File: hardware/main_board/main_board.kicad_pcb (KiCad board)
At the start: 4 copper layers, 154 x 50 mm, 154 parts, among them J1 USB_C_Receptacle_USB2.0_16P, J2 UART_DEBUG, J3 BAT1, J4 Conn_02x05_Odd_Even, J5 Conn_02x05_Odd_Even, Q1 MMBT3904, Q10 MMBTA42, Q11 MMBTA92, Q12 MMBTA42, Q13 MMBTA92, Q14 MMBTA42, Q15 MMBTA92, Q2 MMBT3904, Q3 FDS2734, Q4 MMBTA92, Q5 MMBTA42, Q6 MMBTA42, Q7 MMBTA92, Q8 MMBTA42, Q9 MMBTA92, SW1 SW_Push, U1 MPU-6050, U10 AMS1117, U11 LM5155, U12 IP5305T, U13 74HC238, U2 CP2102N-A02-GQFN28, U3 SRV05-4, U4 DFPlayer_mini, U5 ESP32-S3-WROOM1, U6 DS3231MZ, U7 INA3221, U8 BQ27441DRZR-G1A, U9 TPS62177DQC

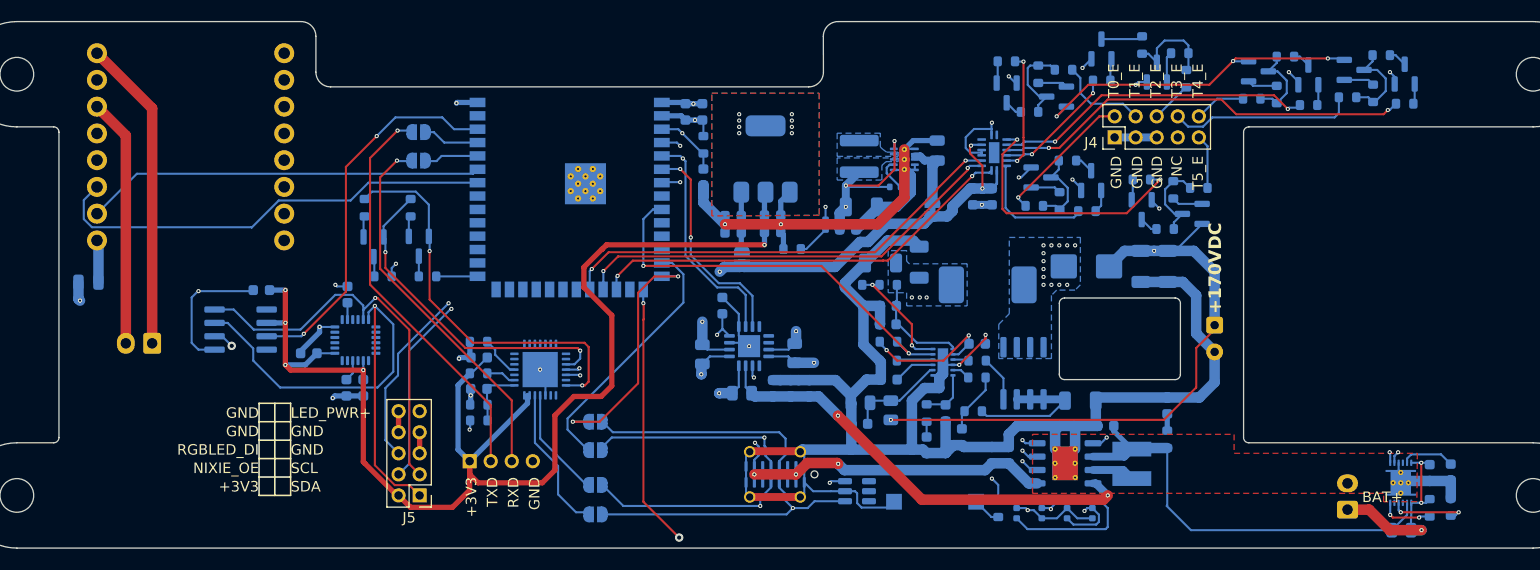
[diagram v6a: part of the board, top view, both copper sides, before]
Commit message: hardware(schematic): update main control board schematic and layout
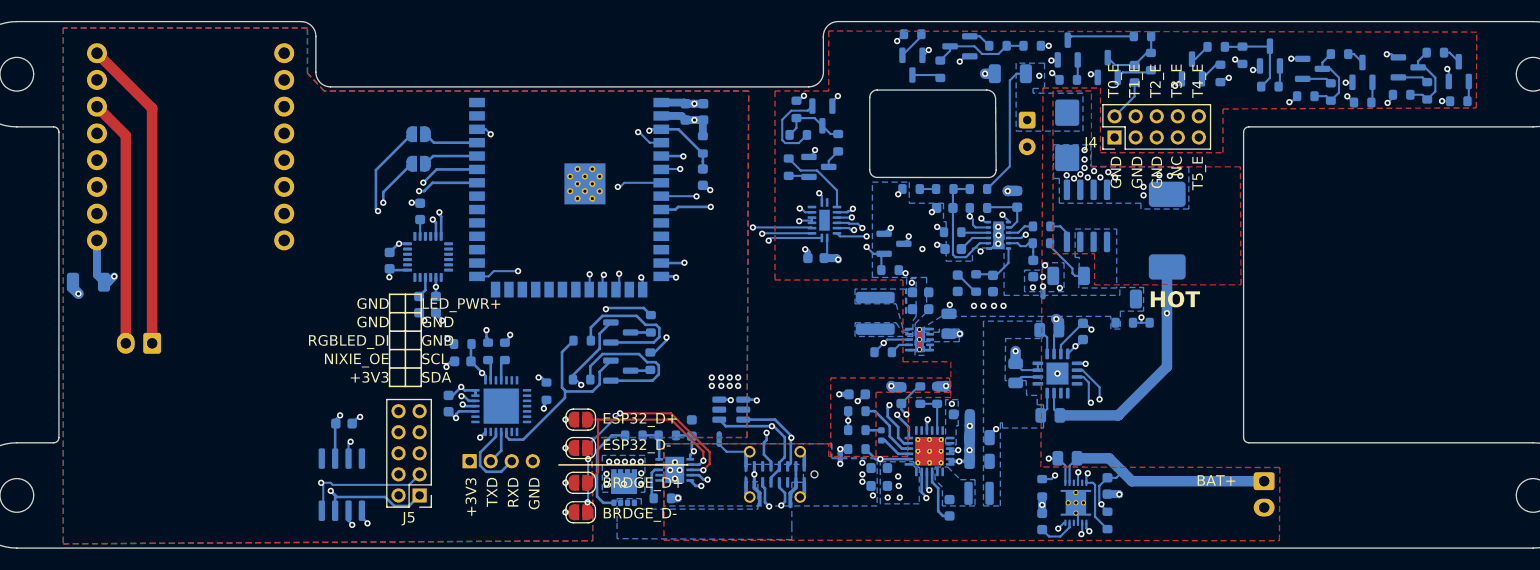
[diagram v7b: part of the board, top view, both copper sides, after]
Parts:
- removed C12, C22, C23, C28, C42, C43: 0.1u, Capacitor_SMD:C_0603_1608Metric
- removed C15: 22u, Capacitor_SMD:C_0603_1608Metric
- removed C24, C27: 10u, Capacitor_SMD:C_0603_1608Metric
- removed C26: 100u, Capacitor_SMD:C_1206_3216Metric
- removed C35: 0.47u/200V, Capacitor_SMD:C_1206_3216Metric
- removed D1, D2, D3: LED, LED_SMD:LED_0402_1005Metric
- removed D5: R_LED, LED_SMD:LED_0402_1005Metric
- removed the G*** at (97.6, 134.9)
- removed JP7: NC, Jumper:SolderJumper-2_P1.3mm_Bridged_RoundedPad1.0x1.5mm
- removed JP8: NO, Jumper:SolderJumper-2_P1.3mm_Open_RoundedPad1.0x1.5mm
- removed L1: PRS4018-2R2NT, johnson:L_SMD_4040
- removed R15: 2, Resistor_SMD:R_0603_1608Metric
- removed R22: 10k, Resistor_SMD:R_0603_1608Metric
- removed SW1: SW_Push, Button_Switch_SMD:SW_SPST_CK_RS282G05A3
- removed U12: IP5305T, Package_SO:HTSOP-8-1EP_3.9x4.9mm_P1.27mm_EP2.4x3.2mm_ThermalVias
- added C44: 4.7u, Capacitor_SMD:C_0603_1608Metric, B.Cu at (158.0, 131.5)
- added C45: 10u, Capacitor_SMD:C_0603_1608Metric, B.Cu at (163.7, 133.3)
- added C46: 10u, Capacitor_SMD:C_0805_2012Metric, B.Cu at (165.4, 137.8)
- added C47: 10u, Capacitor_SMD:C_0805_2012Metric, B.Cu at (165.4, 135.5)
- added G***: LOGO, habonroof_kicad_library:HR_logo_6mmx6mm, B.Cu at (100.2, 125.5)
- added L4: 1u, Inductor_SMD:L_Wuerth_PMCI-252010, B.Cu at (165.4, 140.8)
- added NT1: NetTie_2, NetTie:NetTie-2_SMD_Pad0.5mm, B.Cu at (152.2, 137.5)
- added NT2: NetTie_2, NetTie:NetTie-2_SMD_Pad0.5mm, B.Cu at (140.7, 135.7)
- added NT3: NetTie_2, NetTie:NetTie-2_SMD_Pad0.5mm, B.Cu at (171.4, 121.7)
- added Q16: 2N7002, Package_TO_SOT_SMD:SOT-23, B.Cu at (157.3, 117.1)
- added Q17: FDMC4435BZ, Package_SON:VSON-8_3.3x3.3mm_P0.65mm_NexFET, B.Cu at (131.7, 140.3)
- added R3: 150, Resistor_SMD:R_0603_1608Metric, B.Cu at (158.9, 111.9)
- added R4: 100k, Resistor_SMD:R_0603_1608Metric, B.Cu at (156.9, 119.6)
- added R57: 100k, Resistor_SMD:R_0603_1608Metric, B.Cu at (135.8, 135.3)
- added R58: 10k, Resistor_SMD:R_0603_1608Metric, B.Cu at (135.3, 141.3)
- added R62: 10k, Resistor_SMD:R_0603_1608Metric, B.Cu at (153.8, 136.6)
- added R63: 10k, Resistor_SMD:R_0603_1608Metric, B.Cu at (159.8, 131.5)
- added R64: 10k, Resistor_SMD:R_0603_1608Metric, B.Cu at (161.4, 131.5)
- added R66: 2.2k, Resistor_SMD:R_0603_1608Metric, B.Cu at (153.8, 134.8)
- added U14: BQ25601, Package_DFN_QFN:Texas_RTW_WQFN-24-1EP_4x4mm_P0.5mm_EP2.7x2.7mm_ThermalVias, B.Cu at (160.7, 136.8)
- C10, C11, C21: value 10u -> 1u
- C17, C4, C40, C5: value 0.1u -> 100n
- C18: value 22u -> 10u
- C20: value 22u -> 47n
- C30: value 18n -> 120n
- C31: value 33p -> 50p
- C32: value 1n -> 100n
- C39: footprint Capacitor_SMD:C_1206_3216Metric -> Capacitor_SMD:C_0603_1608Metric
- C7: value 100uF -> 100u; footprint Capacitor_SMD:C_0805_2012Metric -> Capacitor_SMD:C_1206_3216Metric
- C8: value 0.1u -> 1u
- D4: value LED -> GLED
- JP1, JP2, JP5, JP6: moved to F.Cu
- R19: footprint Resistor_SMD:R_0402_1005Metric -> Resistor_SMD:R_0603_1608Metric
- R27: value 30k -> 22k
- R28: value 0 -> 10k
- R29: value 0 -> 10
- R30: value 0 -> 100
- R31: value LMJ12MF1P0R047 -> WSLP1206R0330FEA
- R32: footprint Resistor_SMD:R_0805_2012Metric -> Resistor_SMD:R_0603_1608Metric
- R33: value 6k -> 5.6k; footprint Resistor_SMD:R_0805_2012Metric -> Resistor_SMD:R_0603_1608Metric
- U10: value AMS1117 -> HUSB238_002DD; footprint Package_TO_SOT_SMD:SOT-223-3_TabPin2 -> Package_DFN_QFN:WDFN-10-1EP_3x3mm_P0.5mm_EP1.8x2.5mm
- moved C11 78.2 mm to (105.1, 134.2), turned to 0 degrees
- moved C13 39.1 mm to (171.4, 143.5), turned to 90 degrees
- moved R56 38.9 mm to (148.0, 104.3), turned to 90 degrees
- moved R20 38.8 mm to (171.4, 140.3), turned to 90 degrees
- moved Q15 36.3 mm to (150.5, 105.0), turned to -90 degrees
- moved R55 36.0 mm to (148.2, 106.8), turned to 180 degrees
- moved R53 33.5 mm to (147.3, 109.8), turned to -90 degrees
- moved R28 33.0 mm to (132.6, 135.3), turned to 0 degrees
- moved R12 33.0 mm to (172.1, 125.3), turned to 0 degrees
- moved R16 32.4 mm to (173.8, 137.5)
- moved R54 32.1 mm to (152.0, 107.5), turned to 90 degrees
- moved Q14 30.9 mm to (150.2, 109.8), turned to 0 degrees
- moved U8 30.9 mm to (174.6, 141.7), turned to 90 degrees
- moved U10 30.8 mm to (136.5, 138.6), turned to 180 degrees
- moved C19 30.6 mm to (177.6, 140.1)
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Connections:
- C10 pad 1: Net-(U12-BAT) -> +5V
- C11 pad 1: Net-(C11-Pad1) -> +3V3
- C13 pad 2: GND -> PGND1
- C18 pad 1: +5V_CHG -> Net-(U14-PMID)
- C18 pad 2: GND -> AGND1
- C19 pad 2: GND -> PGND1
- C20 pad 1: +5V_CHG -> Net-(C20-Pad1)
- C20 pad 2: GND -> Net-(U14-BTST)
- C21 pad 1: Net-(JP8-B) -> VBUS
- C25 pad 2: GND -> PGND1
- C29 pad 2: GND -> PGND1
- C30 pad 2: GND -> PGND1
- C31 pad 2: GND -> PGND1
- C32 pad 1: Net-(C32-Pad1) -> Net-(U11-CS)
- C32 pad 2: GND -> PGND2
- C33 pad 1: GND -> PGND1
- C34 pad 2: GND -> PGND2
- C36 pad 2: GND -> PGND2
- C37 pad 2: GND -> PGND1
- C38 pad 1: Net-(JP7-B) -> +5V
- C38 pad 2: GND -> PGND1
- C39 pad 2: GND -> PGND1
- C40 pad 2: GND -> PGND1
- C41 pad 2: GND -> PGND1
- C8 pad 1: VBUS -> Net-(Q17-D)
- C8 pad 2: GND -> PGND1
- C9 pad 1: VBUS -> Net-(Q17-D)
- C9 pad 2: GND -> PGND1
- J1 pad A1: GND -> PGND1
- J1 pad A12: GND -> PGND1
- J1 pad A5: unconnected-(J1-CC1-PadA5) -> Net-(J1-CC1)
- J1 pad B1: GND -> PGND1
- J1 pad B12: GND -> PGND1
- J1 pad B5: unconnected-(J1-CC2-PadB5) -> Net-(J1-CC2)
- J1 pad S1: GND -> PGND1
- J3 pad 2: GND -> PGND1
- J4 pad 1: GND -> PGND1
- J4 pad 3: GND -> PGND1
- J4 pad 5: GND -> PGND1
- Q10 pad 2: GND -> PGND1
- Q12 pad 2: GND -> PGND1
- Q14 pad 2: GND -> PGND1
- Q5 pad 2: GND -> PGND1
- Q6 pad 2: GND -> PGND1
- Q8 pad 2: GND -> PGND1
- R1 pad 2: VBUS -> VSYS
- R10 pad 2: +5V -> VSYS
- R11 pad 1: +5V -> VSYS
- R11 pad 2: +5V_CHG -> +5V
- R12 pad 1: LED_PWR+ -> VSYS
- R12 pad 2: +5V -> LED_PWR+
- R16 pad 1: Net-(U12-BAT) -> Net-(U8-SRN)
- R20 pad 1: GND -> PGND1
- R24 pad 2: GND -> PGND1
- R25 pad 2: GND -> PGND1
- R28 pad 1: Net-(C32-Pad1) -> Net-(Q17-G)
- R28 pad 2: Net-(U11-CS) -> Net-(U10-GATE)
- R30 pad 2: Net-(C32-Pad1) -> Net-(U11-CS)
- R31 pad 2: GND -> PGND2
- R33 pad 2: GND -> Net-(R3-Pad1)
- R9 pad 1: Net-(R9-Pad1) -> VSYS
- U10 pad 1: GND -> VBUS
- U10 pad 2: +3V3 -> USB_D+
- U10 pad 3: Net-(JP8-B) -> USB_D-
- U11 pad 13: GND -> PGND1
- U11 pad 4: GND -> PGND2
- U11 pad 7: GND -> PGND1
- U13 pad 4: GND -> PGND1
- U13 pad 5: GND -> PGND1
- U13 pad 8: GND -> PGND1
- U3 pad 1: USB_D- -> USB_D+
- U3 pad 3: USB_D+ -> USB_D-
- U3 pad 4: unconnected-(U3-IO3-Pad4) -> Net-(J1-CC2)
- U3 pad 6: unconnected-(U3-IO4-Pad6) -> Net-(J1-CC1)
- U5 pad 8: unconnected-(U5-IO15-Pad8) -> HV_EN
- U7 pad 1: LED_PWR+ -> VSYS
- U7 pad 12: +5V -> VSYS
- U7 pad 14: +5V -> VSYS
- U7 pad 15: +5V_CHG -> +5V
- U7 pad 2: +5V -> LED_PWR+
- U8 pad 13: GND -> PGND1
- U8 pad 3: GND -> PGND1
- U8 pad 7: VBAT -> Net-(U8-SRN)
- U8 pad 8: Net-(U12-BAT) -> VBAT
- U9 pad 1: GND -> PGND1
- U9 pad 11: GND -> PGND1
- U9 pad 2: Net-(JP7-B) -> +5V
- U9 pad 3: Net-(JP7-B) -> +5V
- U9 pad 4: GND -> PGND1
- U9 pad 5: GND -> PGND1
- U9 pad 6: GND -> PGND1
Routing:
- net GND: track 337.6 -> 64.7 mm, vias 23 -> 24
- net /nixie_anode_mux/T5_E: track 5.14 -> 96.1 mm, vias 0 -> 1
- net VSYS: track 0.00 -> 88.1 mm, vias 0 -> 4
- net VBUS: track 68.9 -> 18.8 mm, vias 5 -> 2
- net /hv_power/PWR_HV+: track 120.4 -> 75.3 mm
- net T2_B: track 11.8 -> 56.8 mm
- net I2C0_SDA: track 202.9 -> 158.2 mm, vias 4 -> 6
- net +5V_CHG: track 42.9 -> 0.00 mm, vias 2 -> 0
- net Net-(U12-BAT): track 41.5 -> 0.00 mm
- net PGND1: track 0.00 -> 39.3 mm, vias 0 -> 41
- net T3_B: track 40.0 -> 78.2 mm
- net BAT_LOW: track 98.5 -> 61.9 mm, vias 4 -> 2
- net T4_B: track 30.5 -> 66.5 mm
- net VBAT: track 135.5 -> 102.8 mm, vias 4 -> 3
- net +3V3: track 183.2 -> 150.9 mm, vias 18 -> 8
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- added copper zone on B.Cu, net +5V
- added copper zone on In1.Cu, net +5V
- added copper zone on B.Cu, net /hv_power/PWR_HV+
- added copper zone on F.Cu, net AGND1
- added copper zone on B.Cu, net GND
- added copper zone on In1.Cu, net GND
- added copper zone on B.Cu, net Net-(C20-Pad1)
- added copper zone on F.Cu, net Net-(D6-A)
- added copper zone on B.Cu, net Net-(Q17-D)
- added copper zone on In1.Cu, net Net-(Q17-D)
- added copper zone on In2.Cu, net Net-(Q17-D)
- added copper zone on B.Cu, net Net-(Q3-S-Pad1)
- added copper zone on B.Cu, net Net-(U8-SRN)
- added copper zone on In1.Cu, net Net-(U8-SRN)
- added copper zone on B.Cu, net PGND1
- added copper zone on F.Cu, net PGND1
- added copper zone on In1.Cu, net PGND1
- added copper zone on B.Cu, net PGND2
- added copper zone on In1.Cu, net PGND2
- added copper zone on B.Cu, net VBUS
- added copper zone on B.Cu, net VSYS
- removed copper zone on F.Cu, net +3V3
- removed copper zone on In2.Cu, net GND
- removed copper zone on B.Cu, net HV_PWR+
- removed copper zone on In1.Cu, net Net-(D6-A)
- removed copper zone on In2.Cu, net Net-(D6-A)
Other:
- outline, holes or cut-outs redrawn
- board text added: "HOT"
- board text added: "Main board V0.9.0"
- board text removed: "+170VDC"
- board text removed: "170VDC"
- board text removed: "BUCK3V3"
- board text removed: "LDO3V3"
- board text removed: "Nixie Clock V1.9.0"

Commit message: chore(sch): adjust 3v3, 5v and power switch solutions.
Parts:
- removed C32: 100n, Capacitor_SMD:C_0603_1608Metric
- removed C33: 1u, Capacitor_SMD:C_0603_1608Metric
- removed C34: 0.1u/200V, Capacitor_SMD:C_1206_3216Metric
- removed C36: 10u/400v, johnson:Cap_THT_D8.0mm_L12mm_Horizontal
- removed C37: NC, Capacitor_SMD:C_0603_1608Metric
- removed C47: 10u, Capacitor_SMD:C_0805_2012Metric
- removed D6: ES5EB, Diode_SMD:D_SMB
- removed J2: UART_DEBUG, Connector_PinHeader_2.00mm:PinHeader_1x04_P2.00mm_Horizontal
- removed L2: PSPMAA0805-100M-ANP, johnson:PowerInductor_8mmx8.5mm
- removed NT3: NetTie_2, NetTie:NetTie-2_SMD_Pad0.5mm
- removed Q16: 2N7002, Package_TO_SOT_SMD:SOT-23
- removed Q3: FDS2734, Package_SO:SOIC-8_3.9x4.9mm_P1.27mm
- removed R23: 50k, Resistor_SMD:R_0603_1608Metric
- removed R24: 25k, Resistor_SMD:R_0603_1608Metric
- removed R25: 220k, Resistor_SMD:R_0603_1608Metric
- removed R26: 10k, Resistor_SMD:R_0603_1608Metric
- removed R27: 22k, Resistor_SMD:R_0603_1608Metric
- removed R29: 10, Resistor_SMD:R_0603_1608Metric
- removed R30: 100, Resistor_SMD:R_0603_1608Metric
- removed R31: WSLP1206R0330FEA, Resistor_SMD:R_1206_3216Metric
- removed R32: 1M, Resistor_SMD:R_0603_1608Metric
- removed R33: 5.6k, Resistor_SMD:R_0603_1608Metric
- added C12: 1u, Capacitor_SMD:C_0603_1608Metric, B.Cu at (173.4, 180.4)
- added C15: 0.47u, Capacitor_SMD:C_0603_1608Metric, B.Cu at (173.4, 182.9)
- added C22: 22u, Capacitor_SMD:C_Elec_5x5.4, B.Cu at (148.9, 127.8)
- added C23: 47u, Capacitor_SMD:C_Elec_5x5.4, B.Cu at (142.1, 125.2)
- added C24: NC, Capacitor_SMD:C_0603_1608Metric_Pad1.08x0.95mm_HandSolder, B.Cu at (183.8, 174.7)
- added C26: 100nF, Capacitor_SMD:C_0603_1608Metric, B.Cu at (196.0, 156.7)
- added C27: 22u, Capacitor_SMD:C_0805_2012Metric, B.Cu at (112.7, 181.7)
- added C28: 100u, Capacitor_SMD:C_Elec_6.3x5.4, B.Cu at (91.9, 123.0)
- added C42: 470p, Capacitor_SMD:C_0603_1608Metric, B.Cu at (173.4, 164.2)
- added C43: 1u, Capacitor_SMD:C_0603_1608Metric, B.Cu at (173.4, 166.7)
- added C48: 0.1u/250V, Capacitor_SMD:C_1206_3216Metric, B.Cu at (172.6, 175.5)
- added C50: NC, Capacitor_SMD:C_0603_1608Metric, B.Cu at (173.4, 169.2)
- added Csnub1: NC, Capacitor_SMD:C_0603_1608Metric, B.Cu at (108.5, 152.6)
- added D1: STTH1R06B, Diode_SMD:D_SMB, B.Cu at (170.5, 102.8)
- added D2: RLED, LED_SMD:LED_0603_1608Metric, B.Cu at (137.7, 166.0)
- added D3: RLED, LED_SMD:LED_0603_1608Metric, B.Cu at (137.7, 168.0)
- added L1: 1u, Inductor_SMD:L_Coilcraft_XAL6030-XXX, B.Cu at (184.3, 134.9)
- added L5: ER9.5 Transformer, KiCad_Library:Transformer_ER9.5_11.6mmx8.2mm, B.Cu at (182.7, 116.9)
- added NT4: NetTie_2, NetTie:NetTie-2_SMD_Pad0.5mm, B.Cu at (168.6, 174.5)
- added Q19: FDS2734, Package_SO:SOIC-8_3.9x4.9mm_P1.27mm, B.Cu at (154.2, 156.1)
- added R15: 10k, Resistor_SMD:R_0603_1608Metric, B.Cu at (173.4, 185.4)
- added R22: 10m 50ppm, Resistor_SMD:R_0805_2012Metric, B.Cu at (169.2, 185.2)
- added R59: 42.2k, Capacitor_SMD:C_0603_1608Metric, B.Cu at (196.0, 169.2)
- added R60: 10k, Capacitor_SMD:C_0603_1608Metric, B.Cu at (192.0, 156.7)
- added R61: 115k, Capacitor_SMD:C_0603_1608Metric, B.Cu at (192.0, 159.2)
- added R65: 10k, Capacitor_SMD:C_0603_1608Metric, B.Cu at (192.0, 161.7)
- added R67: 10k, Capacitor_SMD:C_0603_1608Metric, B.Cu at (192.0, 164.2)
- added R68: 10k, Capacitor_SMD:C_0603_1608Metric, B.Cu at (192.0, 166.7)
- added R69: 20k, Capacitor_SMD:C_0603_1608Metric, B.Cu at (192.0, 169.2)
- added R70: 34.8k, Capacitor_SMD:C_0603_1608Metric, B.Cu at (188.0, 156.7)
- added R72: 510k, Capacitor_SMD:C_0603_1608Metric, B.Cu at (188.0, 159.2)
- added R73: 91k, Capacitor_SMD:C_0603_1608Metric, B.Cu at (188.0, 161.7)
- added R74: 50k, Resistor_SMD:R_0603_1608Metric, B.Cu at (169.4, 159.2)
- added R75: 25k, Resistor_SMD:R_0603_1608Metric, B.Cu at (169.4, 161.7)
- added R76: 43k, Resistor_SMD:R_0603_1608Metric, B.Cu at (169.4, 164.2)
- added R77: 10k, Resistor_SMD:R_0603_1608Metric, B.Cu at (169.4, 166.7)
- added R78: 22k, Resistor_SMD:R_0603_1608Metric, B.Cu at (169.4, 169.2)
- added R79: 10, Resistor_SMD:R_0603_1608Metric, B.Cu at (165.4, 156.7)
- added R80: 100, Resistor_SMD:R_0603_1608Metric, B.Cu at (165.4, 159.2)
- added R81: WSLP1206R0330FEA, Resistor_SMD:R_1206_3216Metric, B.Cu at (167.0, 172.1)
- added R82: 499k, Resistor_SMD:R_0603_1608Metric, B.Cu at (165.4, 161.7)
- added R83: 5.6k, Resistor_SMD:R_0603_1608Metric, B.Cu at (165.4, 164.2)
- added R84: 150, Resistor_SMD:R_0603_1608Metric, B.Cu at (165.4, 166.7)
- added R85: 10k, Resistor_SMD:R_0603_1608Metric, B.Cu at (146.6, 168.7)
- added R86: 3.3k, Resistor_SMD:R_0603_1608Metric, B.Cu at (146.6, 171.2)
- added R87: 10k, Resistor_SMD:R_0603_1608Metric, B.Cu at (146.6, 173.8)
- added Rsnub1: NC, Resistor_SMD:R_0603_1608Metric, B.Cu at (108.5, 157.6)
- added U12: TPS2121, Package_DFN_QFN:Texas_VQFN-HR-12_2x2.5mm_P0.5mm_ThermalVias, B.Cu at (179.7, 162.1)
- added U15: TPS63802, habonroof_kicad_library:VSON-10-HR-DLA, B.Cu at (180.3, 154.7)
- added U16: BQ27441DRZR-G1A, Package_SON:Texas_S-PDSO-N12, B.Cu at (174.6, 141.7)
- C10, C19: value 1u -> 22u; footprint Capacitor_SMD:C_0603_1608Metric -> Capacitor_SMD:C_Elec_5x5.4
- C13: value 0.47u -> 10u; footprint Capacitor_SMD:C_0603_1608Metric -> Capacitor_SMD:C_0805_2012Metric
- C25: value 100u -> 10u/400v; footprint Capacitor_SMD:C_1206_3216Metric -> KiCad_Library:Cap_THT_D8.0mm_L12mm_Horizontal
- C29: value 180n -> 1u
- C30: value 120n -> 22n
- C31: value 50p -> 22n
- C38: value 2.2u/35V -> 180n; footprint Capacitor_SMD:C_0805_2012Metric -> Capacitor_SMD:C_0603_1608Metric
- C39: value 22u -> 120n
- C40: value 100n -> 50p
- C7: value 100u -> 10u; footprint Capacitor_SMD:C_1206_3216Metric -> Capacitor_SMD:C_0805_2012Metric
- C9: footprint Capacitor_SMD:C_0603_1608Metric -> Capacitor_SMD:C_0805_2012Metric
- D4: value GLED -> RLED; footprint LED_SMD:LED_0402_1005Metric -> LED_SMD:LED_0603_1608Metric
- L3: value 10uH -> 0.47u; footprint Inductor_SMD:L_Changjiang_FNR4010S -> Capacitor_SMD:C_0603_1608Metric
- R10, R11, R12: value 10m 50ppm -> 4.7k; footprint Resistor_SMD:R_0805_2012Metric -> Resistor_SMD:R_0603_1608Metric
- R16: value 10m 50ppm -> 732k; footprint Resistor_SMD:R_0805_2012Metric -> Resistor_SMD:R_0603_1608Metric
- R17: value 10k -> 100k
- R19: value 100k -> 10k
- R20: value 10k -> 51.1k; footprint Resistor_SMD:R_0603_1608Metric -> Capacitor_SMD:C_0603_1608Metric
- R3: value 150 -> 499k
- R4: value 100k -> 4.7k
- R66: value 2.2k -> 3.3k
- U11: value LM5155 -> TPS22810DBVR; footprint Package_SON:WSON-12-1EP_3x2mm_P0.5mm_EP1x2.65 -> Package_TO_SOT_SMD:SOT-23-6
- U7: value INA3221 -> TPS22918DBVR; footprint Package_DFN_QFN:Texas_RGV0016A_VQFN-16-1EP_4x4mm_P0.65mm_EP2.1x2.1mm -> Package_TO_SOT_SMD:SOT-23-6
- U8: value BQ27441DRZR-G1A -> LM5155; footprint Package_SON:Texas_S-PDSO-N12 -> Package_SON:WSON-12-1EP_3x2mm_P0.5mm_EP1x2.65
- U9: value TPS62177DQC -> TPS61022; footprint Package_SON:WSON-10-1EP_2x3mm_P0.5mm_EP0.84x2.4mm_ThermalVias -> Package_DFN_QFN:Texas_RWU0007A_VQFN-7_2x2mm_P0.5mm
- moved U11 82.4 mm to (107.9, 173.5)
- moved R12 78.1 mm to (116.9, 180.6), turned to 180 degrees
- moved R11 71.2 mm to (116.9, 178.1), turned to 180 degrees
- moved C31 70.3 mm to (116.9, 170.5), turned to 180 degrees
- moved R10 69.5 mm to (116.9, 175.6)
- moved R19 69.2 mm to (122.7, 187.9)
- moved C13 68.4 mm to (112.7, 178.6), turned to 180 degrees
- moved R4 66.8 mm to (116.9, 173.1), turned to 180 degrees
- moved C29 66.4 mm to (116.9, 165.5)
- moved R3 66.4 mm to (108.5, 155.1)
- moved C30 66.2 mm to (116.9, 168.0), turned to 180 degrees
- moved C7 60.9 mm to (112.7, 172.6)
- moved C10 58.1 mm to (119.7, 142.2), turned to 180 degrees
- moved C9 56.0 mm to (112.7, 175.6)
- moved L3 53.8 mm to (196.0, 159.2), turned to 180 degrees
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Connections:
- C10 pad 1: +5V -> VBUS
- C10 pad 2: GND -> PGND1
- C13 pad 1: Net-(U8-V_{DD}) -> VBUS
- C19 pad 1: VBAT -> +5V
- C21 pad 1: VBUS -> Net-(Q17-S)
- C25 pad 1: HV_PWR+ -> /hv_power_flyback/PWR_HV+
- C25 pad 2: PGND1 -> PGND2
- C29 pad 1: Net-(U11-SS) -> Net-(U11-VIN)
- C30 pad 1: Net-(C30-Pad1) -> Net-(U11-CT)
- C31 pad 1: Net-(U11-COMP) -> Net-(U7-CT)
- C31 pad 2: PGND1 -> GND
- C38 pad 1: +5V -> Net-(U8-SS)
- C39 pad 1: +3V3 -> Net-(C39-Pad1)
- C40 pad 1: +3V3 -> Net-(U8-COMP)
- C45 pad 1: Net-(U8-SRN) -> /Gasgauge/CHG
- C7 pad 1: +5V -> VSYS
- C7 pad 2: GND -> PGND1
- C8 pad 1: Net-(Q17-D) -> VBUS
- C9 pad 1: Net-(Q17-D) -> VSYS
- J1 pad A4: VBUS -> Net-(Q17-S)
- J1 pad A9: VBUS -> Net-(Q17-S)
- J1 pad B4: VBUS -> Net-(Q17-S)
- J1 pad B9: VBUS -> Net-(Q17-S)
- L3 pad 1: Net-(U9-SW) -> Net-(U15-L1)
- L3 pad 2: +3V3 -> Net-(U15-L2)
- Q11 pad 2: /hv_power/PWR_HV+ -> /hv_power_flyback/PWR_HV+
- Q13 pad 2: /hv_power/PWR_HV+ -> /hv_power_flyback/PWR_HV+
- Q15 pad 2: /hv_power/PWR_HV+ -> /hv_power_flyback/PWR_HV+
- Q17 pad 1: VBUS -> Net-(Q17-S)
- Q17 pad 5: Net-(Q17-D) -> VBUS
- Q4 pad 2: /hv_power/PWR_HV+ -> /hv_power_flyback/PWR_HV+
- Q7 pad 2: /hv_power/PWR_HV+ -> /hv_power_flyback/PWR_HV+
- Q9 pad 2: /hv_power/PWR_HV+ -> /hv_power_flyback/PWR_HV+
- R10 pad 1: HV_PWR+ -> +3V3
- R10 pad 2: VSYS -> I2C0_SDA
- R11 pad 1: VSYS -> I2C1_SCL
- R11 pad 2: +5V -> +3V3
- R12 pad 1: VSYS -> +3V3
- R12 pad 2: LED_PWR+ -> I2C1_SDA
- R16 pad 1: Net-(U8-SRN) -> +5V
- R16 pad 2: VBAT -> Net-(U9-FB)
- R17 pad 1: VBAT -> Net-(U9-FB)
- R17 pad 2: BAT_LOW -> PGND1
- R19 pad 1: Net-(U9-PG) -> BAT_LOW
- R19 pad 2: +3V3 -> Net-(U16-V_{DD})
- R20 pad 1: PGND1 -> Net-(U12-ILIM)
- R20 pad 2: Net-(U8-BIN) -> PGND1
- R3 pad 1: Net-(R3-Pad1) -> /hv_power_flyback/PWR_HV+
- R3 pad 2: PGND1 -> Net-(R3-Pad2)
- R4 pad 1: HV_EN -> I2C0_SCL
- R4 pad 2: PGND1 -> +3V3
- R57 pad 1: VBUS -> Net-(Q17-S)
- U1 pad 23: I2C0_SCL -> I2C1_SCL
- U1 pad 24: I2C0_SDA -> I2C1_SDA
- U1 pad 9: unconnected-(U1-AD0-Pad9) -> +3V3
- U10 pad 1: VBUS -> Net-(Q17-S)
- U10 pad 9: unconnected-(U10-ISET-Pad9) -> Net-(U10-ISET)
- U11 pad 1: HV_PWR+ -> Net-(U11-VIN)
- U11 pad 2: PWR_HV_VCC -> PGND1
- U11 pad 3: Net-(U11-GATE) -> HV_EN
- U11 pad 4: PGND2 -> HV_PWR+
- U11 pad 5: Net-(U11-CS) -> unconnected-(U11-QOD-Pad5)
- U11 pad 6: Net-(U11-COMP) -> Net-(U11-CT)
- U14 pad 1: Net-(Q17-D) -> VBUS
- U14 pad 13: Net-(U8-SRN) -> /Gasgauge/CHG
- U14 pad 14: Net-(U8-SRN) -> /Gasgauge/CHG
- U14 pad 24: Net-(Q17-D) -> VBUS
- U3 pad 2: GND -> PGND1
- U3 pad 5: unconnected-(U3-VP-Pad5) -> Net-(Q17-S)
- U4 pad 1: +5V -> Net-(U4-Vcc)
- U5 pad 10: unconnected-(U5-IO17-Pad10) -> I2C1_SCL
- U5 pad 11: unconnected-(U5-IO18-Pad11) -> I2C1_SDA
- U5 pad 28: unconnected-(U5-IO35-Pad28) -> 5V_MODE
- U5 pad 29: unconnected-(U5-IO36-Pad29) -> 5V_EN
- U5 pad 9: HV_PG -> DF_EN
- U6 pad 7: I2C0_SDA -> I2C1_SDA
- U6 pad 8: I2C0_SCL -> I2C1_SCL
- U7 pad 1: VSYS -> +5V
- U7 pad 2: LED_PWR+ -> GND
- U7 pad 3: GND -> DF_EN
- U7 pad 4: +5V -> Net-(U4-Vcc)
- U7 pad 5: GND -> unconnected-(U7-QOD-Pad5)
- U7 pad 6: I2C0_SCL -> Net-(U7-CT)
- U8 pad 1: I2C0_SDA -> HV_PWR+
- U8 pad 10: Net-(U8-BIN) -> Net-(U8-RT)
- U8 pad 11: unconnected-(U8-NC-Pad11) -> Net-(U8-PGOOD)
- U8 pad 12: BAT_LOW -> Net-(U8-UVLO/EN/SYNC)
- U8 pad 2: I2C0_SCL -> PWR_HV_VCC
- U8 pad 3: PGND1 -> Net-(U8-GATE)
- U8 pad 4: unconnected-(U8-NC-Pad4) -> PGND2
- U8 pad 5: Net-(U8-V_{DD}) -> Net-(U8-CS)
- U8 pad 6: VBAT -> Net-(U8-COMP)
- U8 pad 7: Net-(U8-SRN) -> PGND1
- U8 pad 8: VBAT -> Net-(U8-FB)
- U8 pad 9: unconnected-(U8-NC-Pad9) -> Net-(U8-SS)
- U9 pad 2: +5V -> Net-(U9-SW)
- U9 pad 4: PGND1 -> Net-(U9-FB)
- U9 pad 5: PGND1 -> 5V_EN
- U9 pad 6: PGND1 -> 5V_MODE
- U9 pad 7: Net-(U9-PG) -> VSYS
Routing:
- net /hv_power/PWR_HV+: track 75.3 -> 0.00 mm, vias 7 -> 0
- net /hv_power_flyback/PWR_HV+: track 0.00 -> 62.3 mm, vias 0 -> 7
- net HV_PG: track 36.5 -> 0.00 mm, vias 2 -> 0
- net DF_EN: track 0.00 -> 36.5 mm, vias 0 -> 2
- net Net-(U8-UVLO/EN/SYNC): track 0.00 -> 34.2 mm, vias 0 -> 3
- net Net-(Q16-D): track 34.2 -> 0.00 mm, vias 3 -> 0
- net (no net): track 0.00 -> 18.8 mm, vias 0 -> 22
- net VBUS: track 18.8 -> 0.00 mm, vias 2 -> 14
- net Net-(Q17-S): track 0.00 -> 18.8 mm, vias 0 -> 2
- net Net-(D1-A): track 0.00 -> 13.0 mm
- net Net-(U8-FB): track 0.00 -> 11.9 mm
- net Net-(U11-FB): track 11.9 -> 0.00 mm
- net Net-(L5-Pad4): track 0.00 -> 7.62 mm
- net PGND1: track 39.3 -> 32.1 mm, vias 41 -> 46
- net GND: track 64.7 -> 59.0 mm, vias 24 -> 13
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- added copper zone on B.Cu, net (none)
- added copper zone on F.Cu, net (none)
- added copper zone on B.Cu, net /Gasgauge/CHG
- added copper zone on In1.Cu, net /Gasgauge/CHG
- added copper zone on B.Cu, net /hv_power_flyback/PWR_HV+
- added copper zone on In1.Cu, net VBUS
- added copper zone on In2.Cu, net VBUS
- removed copper zone on B.Cu, net /hv_power/PWR_HV+
- removed copper zone on In1.Cu, net GND
- removed copper zone on B.Cu, net Net-(D6-A)
- removed copper zone on F.Cu, net Net-(D6-A)
- removed copper zone on B.Cu, net Net-(Q17-D)
- removed copper zone on In1.Cu, net Net-(Q17-D)
- removed copper zone on In2.Cu, net Net-(Q17-D)
- removed copper zone on B.Cu, net Net-(Q3-S-Pad1)
- removed copper zone on B.Cu, net Net-(U8-SRN)
- removed copper zone on In1.Cu, net Net-(U8-SRN)
